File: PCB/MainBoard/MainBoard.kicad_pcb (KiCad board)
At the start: 2 copper layers, 100 x 100 mm, 77 parts, among them J1 Conn_01x01_Socket, J10 Conn_01x06_Socket, J11 Conn_01x06_Socket, J12 Conn_01x04_Socket, J13 Conn_01x01_Socket, J14 Conn_01x03_Socket, J17 Conn_01x02_Socket, J18 Conn_01x04_Socket, J19 Conn_01x04_Socket, J2 Conn_01x01_Socket, J20 Conn_01x04_Socket, J21 Conn_01x02_Socket, J3 Conn_01x01_Socket, J4 Conn_01x02_Socket, J5 Conn_01x03_Socket, J6 Conn_01x03_Socket, J7 Conn_01x03_Socket, J8 Conn_01x02_Socket, J9 Conn_01x02_Socket, SW1 SW_Push, U1 TPS56339DDC, U2 TPS56339DDC, U3 STM32F103C8Tx, U4 CD74HC00_N_14, U5 TPS56339DDC, U6 CD74HC00_N_14

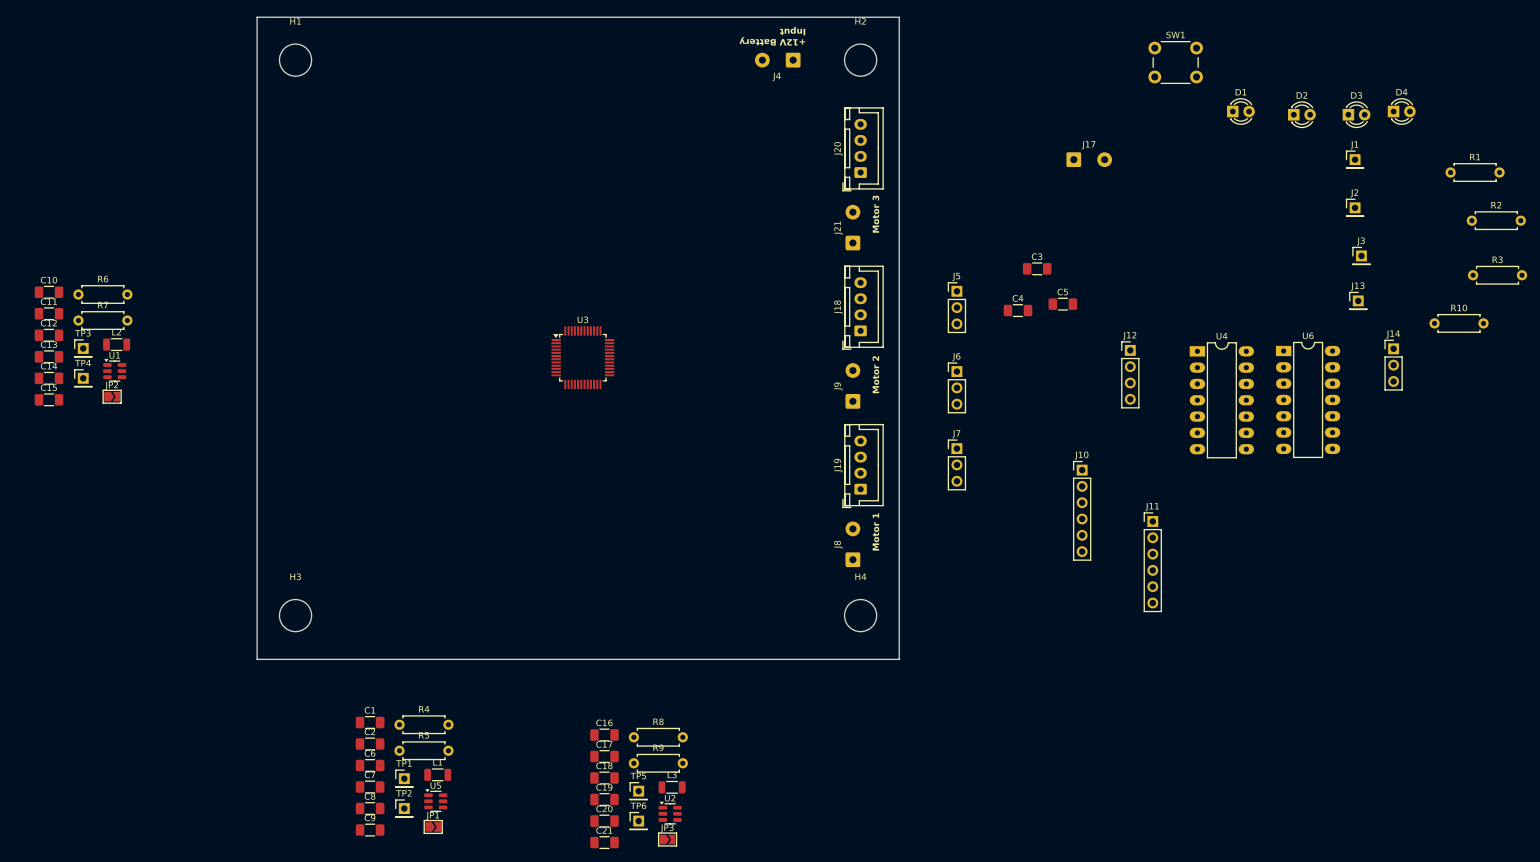
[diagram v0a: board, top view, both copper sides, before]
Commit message: Placed Buck Converters and changed inductors to 1008
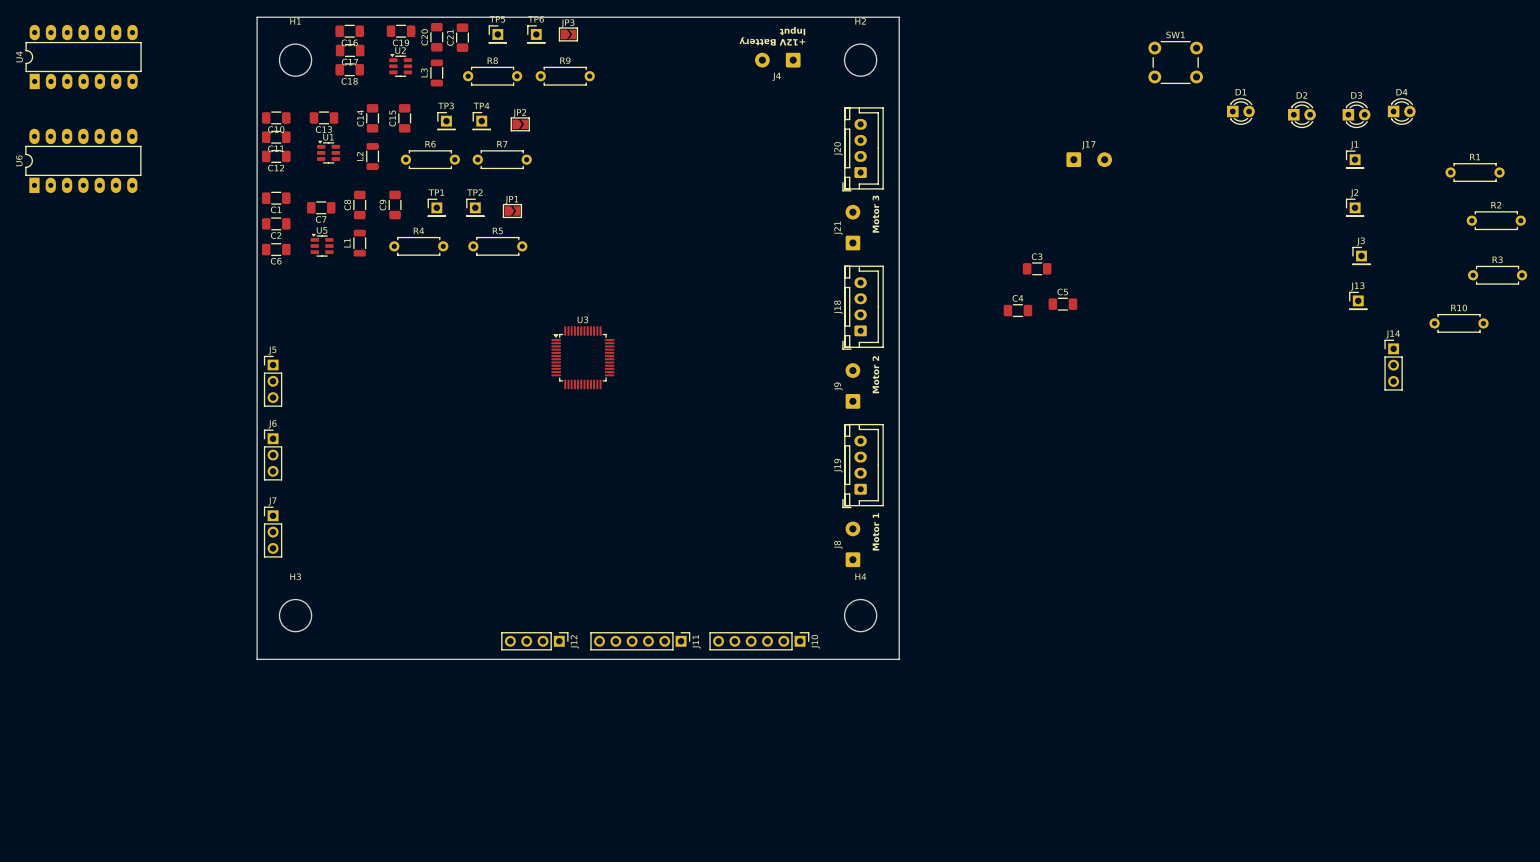
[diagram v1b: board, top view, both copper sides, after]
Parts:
- moved U6 196.2 mm to (67.8, 72.5), turned to 90 degrees
- moved U4 185.9 mm to (67.9, 56.3), turned to 90 degrees
- moved C21 127.3 mm to (134.5, 49.5), turned to 90 degrees
- moved JP3 126.3 mm to (151.0, 49.0)
- moved C20 124.8 mm to (130.5, 49.4), turned to 90 degrees
- moved C19 123.8 mm to (124.9, 48.5), turned to 180 degrees
- moved U2 123.8 mm to (124.9, 54.0)
- moved TP6 123.5 mm to (146.0, 49.0)
- moved TP5 119.9 mm to (140.0, 49.0)
- moved C18 117.2 mm to (116.9, 54.5), turned to 180 degrees
- moved L3 117.1 mm to (130.5, 55.0), turned to 90 degrees
- moved C17 116.9 mm to (117.0, 51.5), turned to 180 degrees
- moved C16 116.6 mm to (116.9, 48.5), turned to 180 degrees
- moved R9 108.0 mm to (146.7, 55.5)
- moved J5 107.1 mm to (105.0, 100.5)
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
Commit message: updated pcb schematic
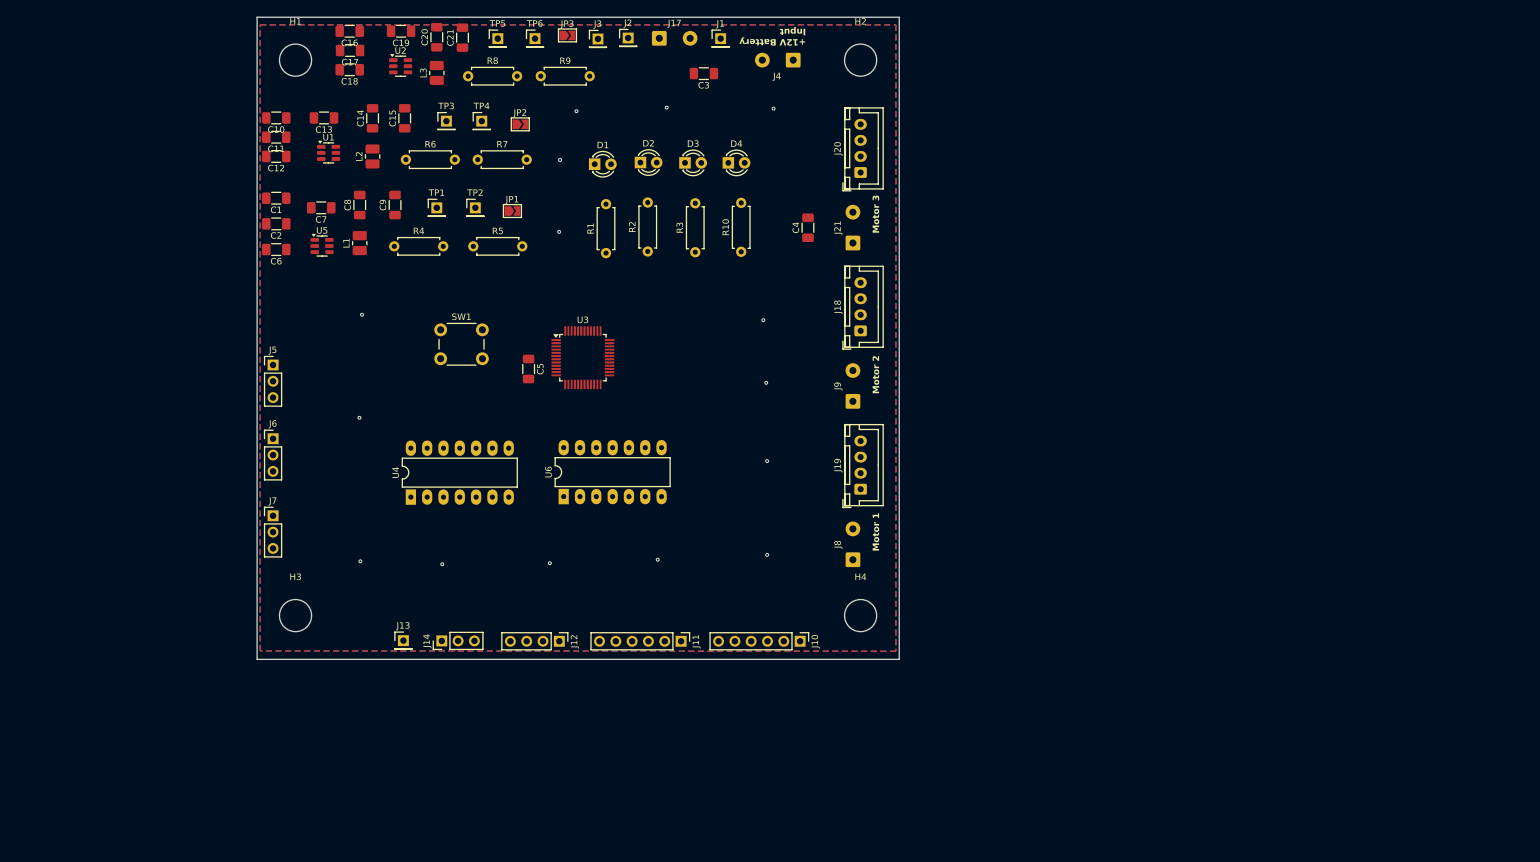
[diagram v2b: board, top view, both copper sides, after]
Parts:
- L1, L2, L3: footprint Inductor_SMD:L_1206_3216Metric -> Inductor_SMD:L_1008_2520Metric_Pad1.43x2.20mm_HandSolder
- moved J13 157.8 mm to (125.3, 143.4)
- moved J14 155.0 mm to (131.3, 143.4), turned to 90 degrees
- moved R1 132.1 mm to (156.8, 83.0), turned to 90 degrees
- moved R2 128.4 mm to (163.3, 82.8), turned to 90 degrees
- moved J3 123.6 mm to (155.6, 49.7)
- moved R3 121.2 mm to (170.8, 82.9), turned to 90 degrees
- moved SW1 119.6 mm to (131.1, 95.0)
- moved J2 116.2 mm to (160.3, 49.5)
- moved R10 108.6 mm to (177.9, 82.8), turned to 90 degrees
- moved D4 103.9 mm to (175.9, 69.0)
- moved D3 103.6 mm to (169.2, 69.0)
- moved D2 102.0 mm to (162.2, 69.0)
- moved J1 100.6 mm to (174.7, 49.6)
- moved D1 99.7 mm to (155.1, 69.2)
- moved U6 95.6 mm to (150.3, 121.0)
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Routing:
- net GND: vias 0 -> 15
- added copper zone on B.Cu, net GND
- added copper zone on F.Cu, net GND

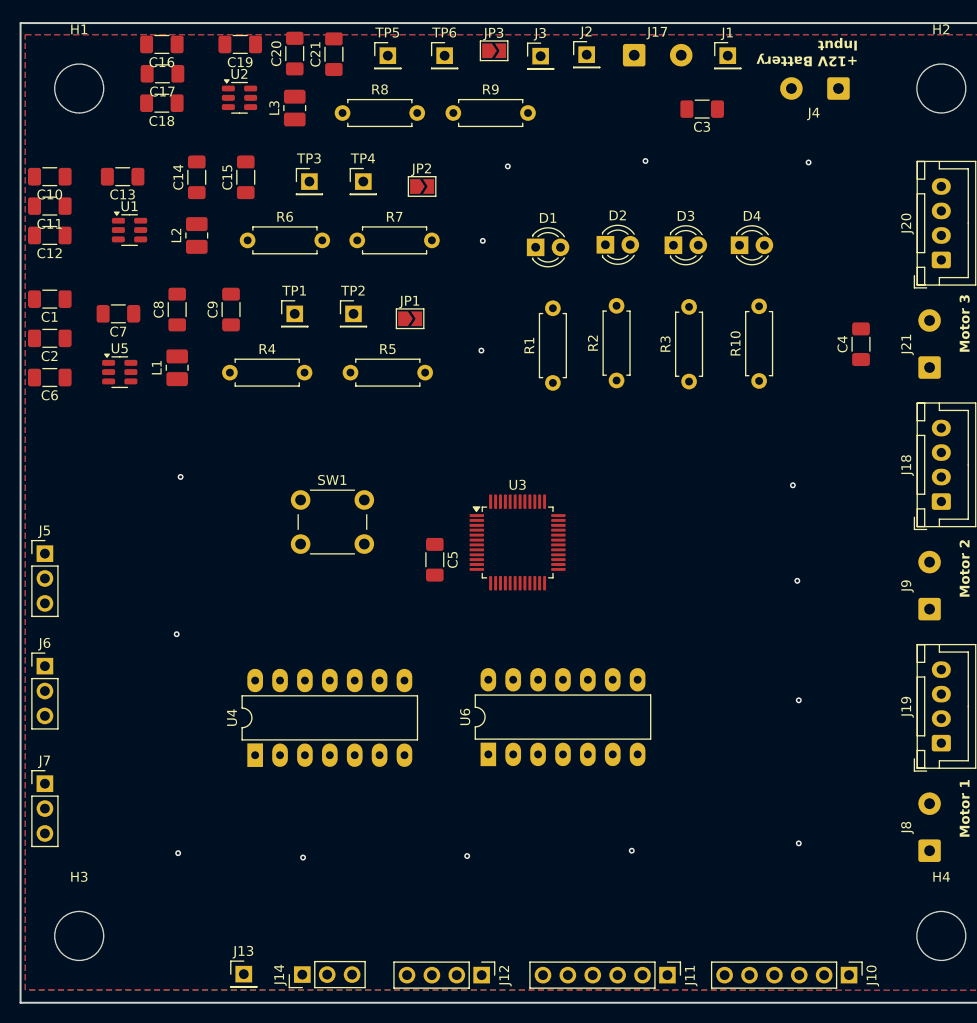
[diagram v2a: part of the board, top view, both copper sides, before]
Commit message: final layout v1 - unconnected
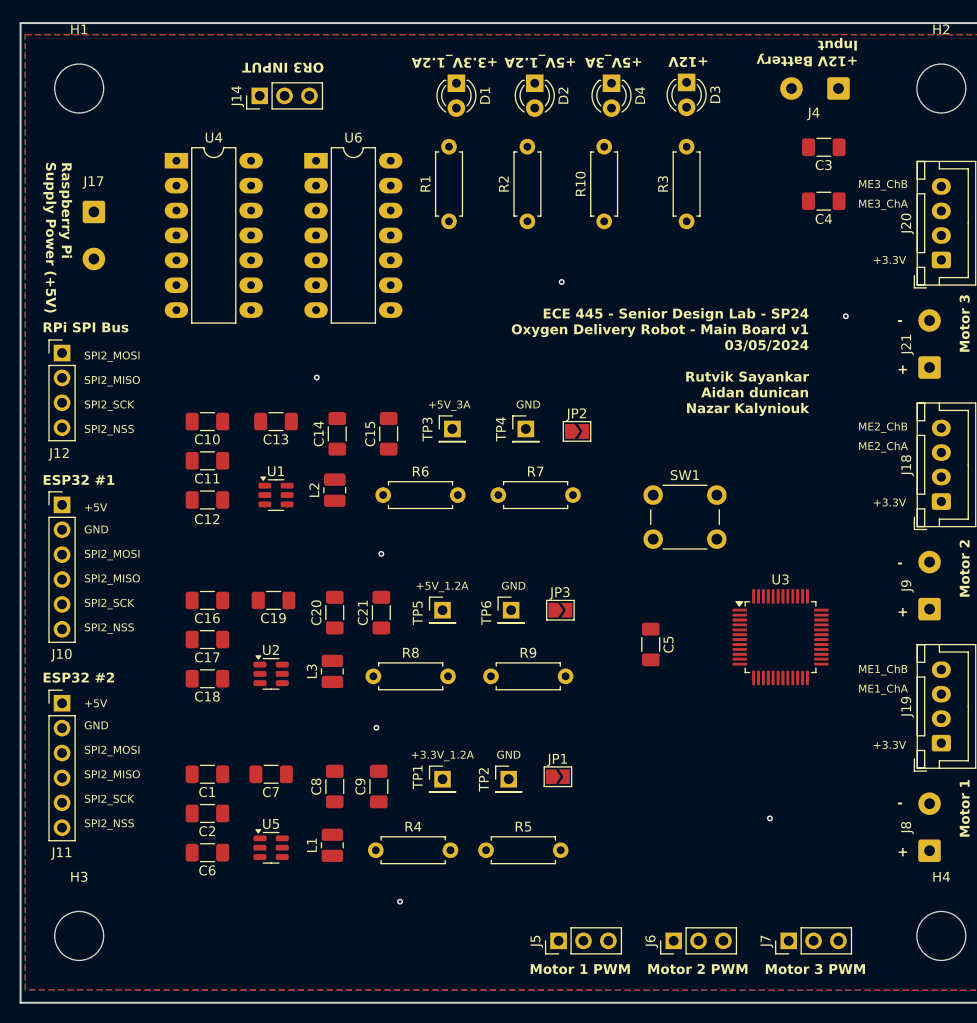
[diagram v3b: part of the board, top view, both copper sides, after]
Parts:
- removed J1, J13, J2, J3: Conn_01x01_Socket, Connector_PinHeader_2.54mm:PinHeader_1x01_P2.54mm_Vertical
- L1, L2, L3: footprint Inductor_SMD:L_1008_2520Metric_Pad1.43x2.20mm_HandSolder -> Inductor_SMD:L_1008_2520Metric
- moved J10 93.6 mm to (106.8, 95.5), turned to 0 degrees
- moved J14 89.8 mm to (126.9, 53.8)
- moved J7 77.6 mm to (180.9, 140.0), turned to 90 degrees
- moved J12 76.6 mm to (106.8, 80.0), turned to 0 degrees
- moved J6 70.0 mm to (169.2, 140.0), turned to 90 degrees
- moved J11 67.7 mm to (106.8, 115.8), turned to 0 degrees
- moved J5 65.7 mm to (157.4, 140.0), turned to 90 degrees
- moved U6 63.1 mm to (132.7, 60.4), turned to 0 degrees
- moved U4 61.2 mm to (118.4, 60.4), turned to 0 degrees
- moved C18 58.9 mm to (121.6, 113.2)
- moved U2 58.9 mm to (128.1, 112.8)
- moved C17 57.9 mm to (121.6, 109.2)
- moved L3 57.6 mm to (134.3, 112.5)
- moved R9 57.6 mm to (150.5, 113.0)
- moved R8 57.6 mm to (138.5, 113.0)
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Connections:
- J5 pad 2: +12V -> +5V_1.2A
- J6 pad 2: +12V -> +5V_1.2A
- J7 pad 2: +12V -> +5V_1.2A
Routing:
- net GND: vias 15 -> 7
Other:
- board text added: "+"
- board text added: "+12V"
- board text added: "+3.3V"
- board text added: "+3.3V_1.2A"
- board text added: "+5V"
- board text added: "+5V_1.2A"
- board text added: "+5V_3A"
- board text added: "-"
- board text added: "ECE 445 - Senior Design Lab - SP24 Oxygen Delivery Robot - Main Board v1 03/05/2024 Rutvik Sayankar Aidan dunican Nazar Kalyniouk"
- board text added: "ESP32 #1"
- board text added: "ESP32 #2"
- board text added: "GND"
- board text added: "ME1_ChA"
- board text added: "ME1_ChB"
- board text added: "ME2_ChA"
- board text added: "ME2_ChB"
- board text added: "ME3_ChA"
- board text added: "ME3_ChB"
- board text added: "Motor 1 PWM"
- board text added: "Motor 2 PWM"
- board text added: "Motor 3 PWM"
- board text added: "OR3 INPUT"
- board text added: "RPi SPI Bus"
- board text added: "Raspberry Pi Supply Power (+5V)"
- board text added: "SPI2_MISO"
- board text added: "SPI2_MOSI"
- board text added: "SPI2_NSS"
- board text added: "SPI2_SCK"

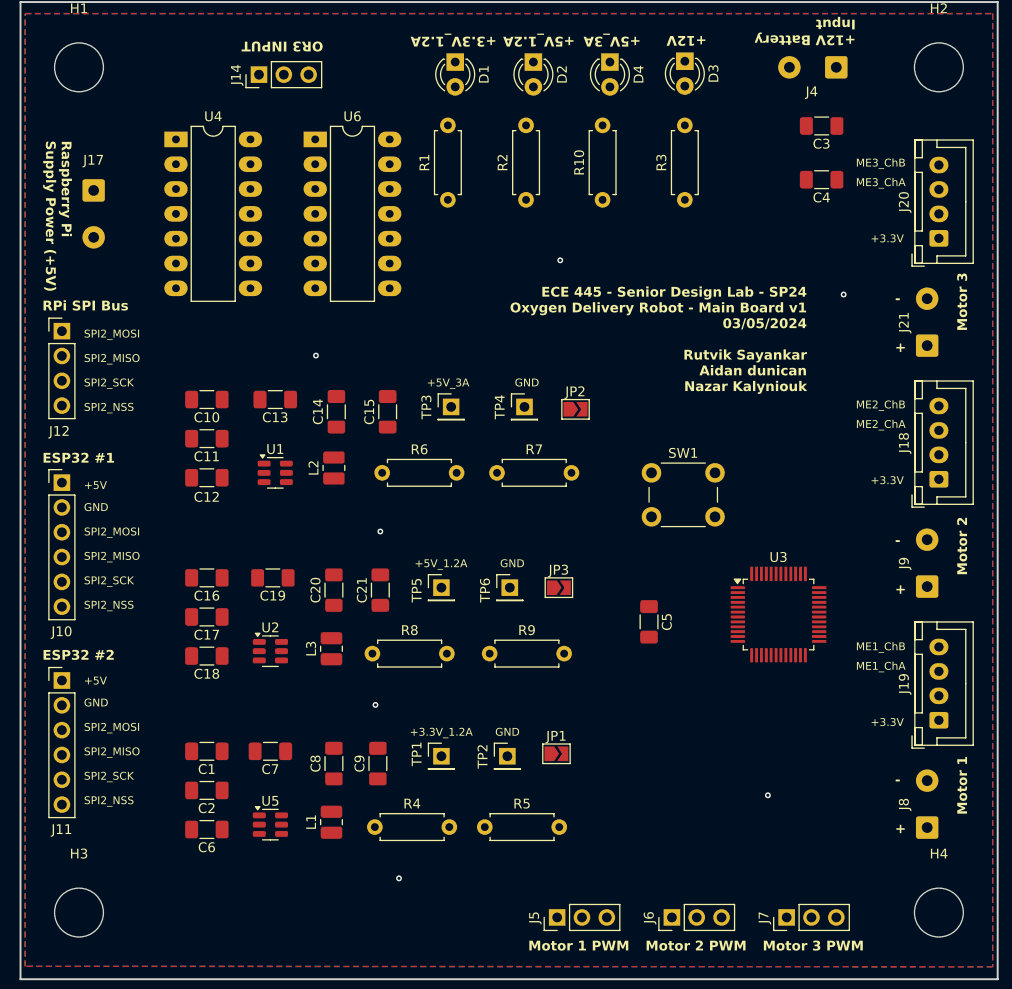
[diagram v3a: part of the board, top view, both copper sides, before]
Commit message: board routed, just need to increase track widths for power lines
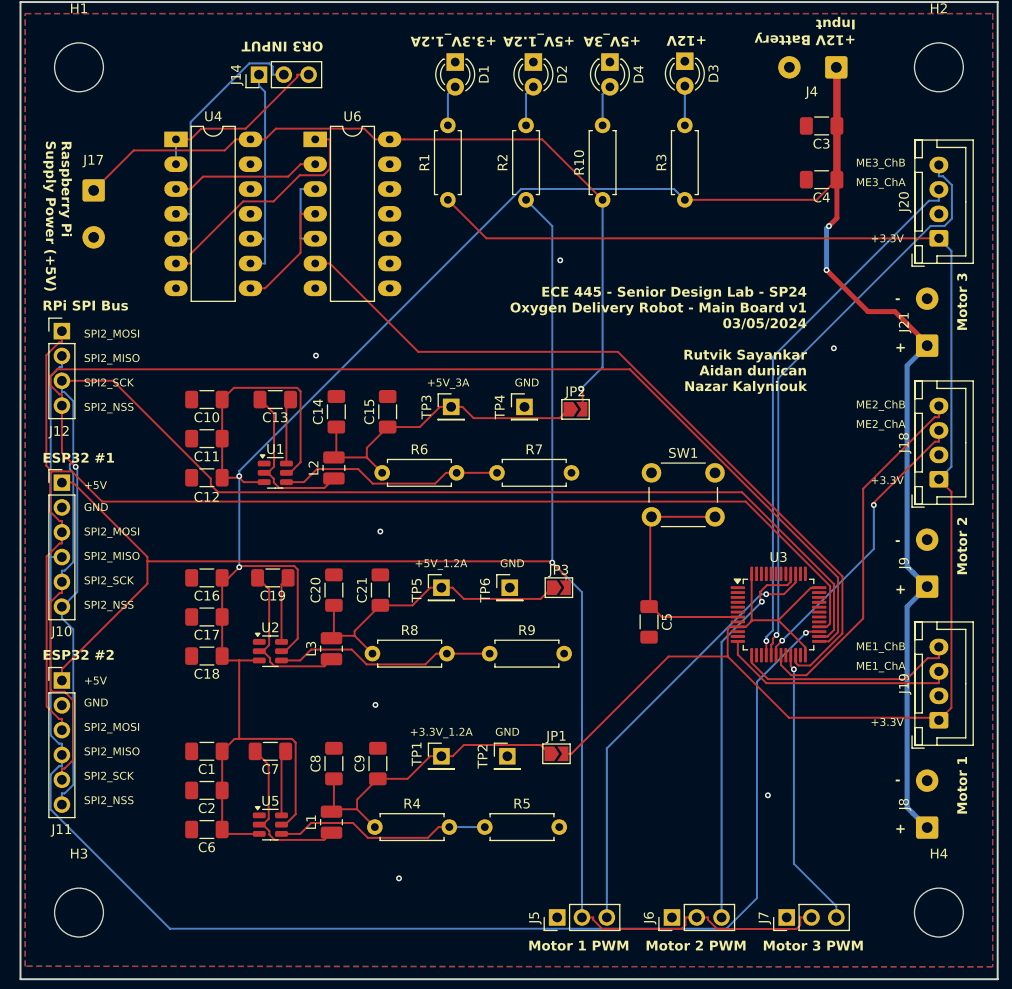
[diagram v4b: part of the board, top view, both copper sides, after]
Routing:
- net +12V: track 0.00 -> 269.4 mm, vias 0 -> 4
- net +5V_1.2A: track 0.00 -> 175.3 mm, vias 0 -> 1
- net +3.3V_1.2A: track 0.00 -> 172.1 mm
- net /SPI2_MISO: track 0.00 -> 158.7 mm, vias 0 -> 1
- net /SPI2_NSS: track 0.00 -> 144.6 mm, vias 0 -> 1
- net /SPI2_SCK: track 0.00 -> 139.9 mm
- net /SPI2_MOSI: track 0.00 -> 133.8 mm
- net +5V_3A: track 0.00 -> 80.1 mm, vias 0 -> 1
- net /LimitSwitchORGates/OR3 Output: track 0.00 -> 80.1 mm
- net /ME3_ChB: track 0.00 -> 59.5 mm, vias 0 -> 1
- net /ME3_ChA: track 0.00 -> 55.6 mm, vias 0 -> 1
- net Net-(J5-Pin_3): track 0.00 -> 44.5 mm, vias 0 -> 1
- net Net-(J6-Pin_3): track 0.00 -> 39.5 mm, vias 0 -> 1
- net /ME2_ChB: track 0.00 -> 37.5 mm
- net Net-(JP2-A): track 0.00 -> 32.9 mm
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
